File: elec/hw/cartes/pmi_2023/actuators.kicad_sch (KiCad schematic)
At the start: 43 parts, among them J1 con_servo, J2 con_servo, J3 con_servo, J4 con_servo, U23 PCA9685PW, U24 SN74LVC1T45DBV, U25 SN74LVC1T45DBV, U26 SN74LVC1T45DBV, U27 SN74LVC1T45DBV

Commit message: front and back tof added, selector changed, ready to route
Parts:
- R54, R55, R56, R57, R58, R59, R60, R61: JLCPCB C21189 -> C431718
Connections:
- net led_vbatt_error: now also BATT_LOW1.1 (K); no longer BATT_LOW1.C
- net at R64.2: now also BATT_LOW1.2 (A); no longer BATT_LOW1.A

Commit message: wip
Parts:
- R62, R63, R64: Specification 1k 0603 1% 100mW -> 10k 0603 1% 100mW; mouser (none) -> 603-RC0603FR-10100KL

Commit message: wip
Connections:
- net led_RGB_b_3v3: now also U23.20 (LED13); no longer U23.21 (LED14)
- net led_RGB_g_3v3: now also U23.21 (LED14); no longer U23.20 (LED13)
- net at R75.2: now also D1.2 (C_GREEN); no longer D1.1 (C_BLUE)
- net at R76.2: now also D1.1 (C_BLUE); no longer D1.2 (C_GREEN)
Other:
- moved on the sheet: R75, R76
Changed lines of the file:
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@@
+	(wire
+		(pts
+			(xy 220.98 50.8) (xy 232.41 50.8)
+		)
+		(stroke
+			(width 0)
+			(type default)
+		)
+	)
 	(wire
 		(pts
@@
 	(wire
 		(pts
-			(xy 229.87 45.72) (xy 232.41 45.72)
-		)
-		(stroke
-			(width 0)
-			(type default)
-		)
-	)
-	(wire
-		(pts
 			(xy 58.42 29.21) (xy 58.42 72.39)
 		)
@@
 	(wire
 		(pts
-			(xy 195.58 50.8) (xy 213.36 50.8)
+			(xy 194.31 45.72) (xy 222.25 45.72)
 		)
 		(stroke
@@
 	(wire
 		(pts
+			(xy 229.87 45.72) (xy 232.41 45.72)
+		)
+		(stroke
+			(width 0)
+			(type default)
+		)
+	)
+	(wire
+		(pts
 			(xy 137.16 21.59) (xy 137.16 29.21)
 		)
@@
 	(wire
 		(pts
-			(xy 220.98 50.8) (xy 232.41 50.8)
-		)
-		(stroke
-			(width 0)
-			(type default)
-		)
-	)
-	(wire
-		(pts
 			(xy 97.79 72.39) (xy 114.3 72.39)
 		)
@@
 	(wire
 		(pts
-			(xy 195.58 45.72) (xy 222.25 45.72)
+			(xy 194.31 50.8) (xy 213.36 50.8)
 		)
 		(stroke
@@
 		)
 	)
-	(label "led_RGB_g_3v3"
+	(label "led_RGB_b_3v3"
 		(at 99.06 69.85 0)
 		(fields_autoplaced yes)
@@
 	)
 	(label "led_RGB_b_3v3"
-		(at 195.58 50.8 0)
+		(at 194.31 45.72 0)
 		(fields_autoplaced yes)
 		(effects
@@
 	)
 	(label "led_RGB_g_3v3"
-		(at 195.58 45.72 0)
+		(at 194.31 50.8 0)
 		(fields_autoplaced yes)
 		(effects
@@
 		)
 	)
-	(label "led_RGB_b_3v3"
+	(label "led_RGB_g_3v3"
 		(at 99.06 72.39 0)
 		(fields_autoplaced yes)
@@
 	(symbol
 		(lib_id "cocotter_resistors:R_51R_0603_1%")
+		(at 226.06 45.72 90)
+		(unit 1)
+		(exclude_from_sim no)
+		(in_bom yes)
+		(on_board yes)
+		(dnp no)
+		(property "Reference" "R75"
+			(at 226.06 43.18 90)
+			(effects
+				(font
+					(size 1.27 1.27)
+				)
+			)
+		)
+		(property "Value" "51R 1%"
+			(at 226.06 48.26 90)
+			(effects
+				(font
+					(size 1.27 1.27)
+				)
+			)
+		)
+		(property "Footprint" "cocotter_resistor:r0603_reflow"
+			(at 226.06 47.498 90)
+			(effects
+				(font
+					(size 1.27 1.27)
+				)
+				(hide yes)
+			)
+		)
+		(property "Datasheet" "~"
+			(at 226.06 45.72 0)
+			(effects
+				(font
+					(size 1.27 1.27)
+				)
+				(hide yes)
+			)
+		)
+		(property "Description" ""
+			(at 226.06 45.72 0)
+			(effects
+				(font
+					(size 1.27 1.27)
+				)
+				(hide yes)
+			)
+		)
+		(property "Specification" "51R 0603 1% 100mW"
+			(at 226.06 45.72 0)
+			(effects
+				(font
+					(size 1.27 1.27)
+				)
+				(hide yes)
+			)
+		)
+		(property "mouser" ""
+			(at 226.06 45.72 0)
+			(effects
+				(font
+					(size 1.27 1.27)
+				)
+				(hide yes)
+			)
+		)
+		(property "JLCPCB" ""
+			(at 226.06 45.72 0)
+			(effects
+				(font
+					(size 1.27 1.27)
+				)
+				(hide yes)
+			)
+		)
+		(pin "2"
+		)
+		(pin "1"
+		)
+		(instances
+			(project "pmi_2023"
+				(path "/334a657f-c66c-4260-9567-14f1c99913d7/76b412a5-2e5b-49f9-bfc4-2fef81997c2b"
+					(reference "R75")
+					(unit 1)
+				)
+			)
+		)
+	)
+	(symbol
+		(lib_id "cocotter_resistors:R_51R_0603_1%")
 		(at 217.17 50.8 90)
 		(unit 1)
@@
 		(on_board yes)
 		(dnp no)
-		(property "Reference" "R75"
+		(property "Reference" "R76"
 			(at 217.17 48.26 90)
 			(effects
@@
 			(effects
 				(font
-					(size 1.27 1.27)
-				)
-				(hide yes)
-			)
-		)
-		(pin "2"
-		)
-		(pin "1"
-		)
-		(instances
-			(project "pmi_2023"
-				(path "/334a657f-c66c-4260-9567-14f1c99913d7/76b412a5-2e5b-49f9-bfc4-2fef81997c2b"
-					(reference "R75")
-					(unit 1)
-				)
-			)
-		)
-	)
-	(symbol
-		(lib_id "cocotter_resistors:R_51R_0603_1%")
-		(at 226.06 45.72 90)
-		(unit 1)
-		(exclude_from_sim no)
-		(in_bom yes)
-		(on_board yes)
-		(dnp no)
-		(property "Reference" "R76"
-			(at 226.06 43.18 90)
-			(effects
-				(font
-					(size 1.27 1.27)
-				)
-			)
-		)
-		(property "Value" "51R 1%"
-			(at 226.06 48.26 90)
-			(effects
-				(font
-					(size 1.27 1.27)
-				)
-			)
-		)
-		(property "Footprint" "cocotter_resistor:r0603_reflow"
-			(at 226.06 47.498 90)
-			(effects
-				(font
-					(size 1.27 1.27)
-				)
-				(hide yes)
-			)
-		)
-		(property "Datasheet" "~"
-			(at 226.06 45.72 0)
-			(effects
-				(font
-					(size 1.27 1.27)
-				)
-				(hide yes)
-			)
-		)
-		(property "Description" ""
-			(at 226.06 45.72 0)
-			(effects
-				(font
-					(size 1.27 1.27)
-				)
-				(hide yes)
-			)
-		)
-		(property "Specification" "51R 0603 1% 100mW"
-			(at 226.06 45.72 0)
-			(effects
-				(font
-					(size 1.27 1.27)
-				)
-				(hide yes)
-			)
-		)
-		(property "mouser" ""
-			(at 226.06 45.72 0)
-			(effects
-				(font
-					(size 1.27 1.27)
-				)
-				(hide yes)
-			)
-		)
-		(property "JLCPCB" ""
-			(at 226.06 45.72 0)
-			(effects
-				(font

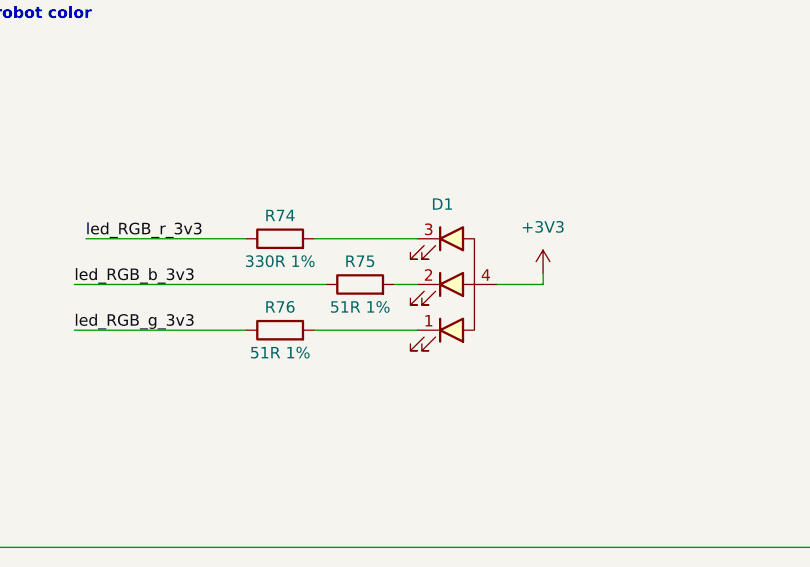
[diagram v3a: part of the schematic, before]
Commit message: added oled display power supply res selectors, jlcpcb refs : wip
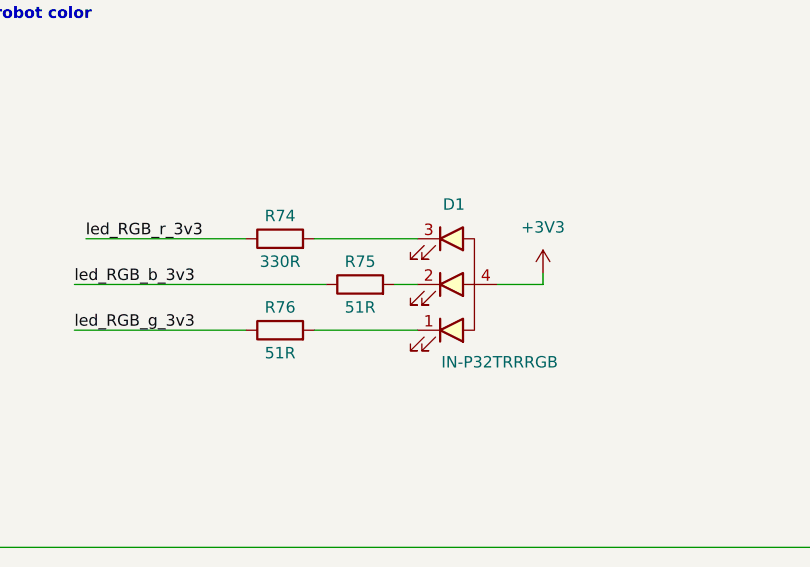
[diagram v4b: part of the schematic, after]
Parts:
- BATT_OK1: value red, 0603 -> white, 0603
- C14, C23, C24, C25, C26: symbol cocotter_capacitors:C_10µF_16V_0805_X5R -> cocotter_capacitors:C_10µF_25V_0805_X5R; Specification 10µF 25V X5R 0805 -> 10µF 25V X7R 0805
- D1: value ~ -> IN-P32TRRRGB; JLCPCB (none) -> C7288909
- R74: value 330R 1% -> 330R; JLCPCB (none) -> C23138
- R75, R76: value 51R 1% -> 51R; JLCPCB (none) -> C23197
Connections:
- net led_vbatt_ok: now also BATT_OK1.1 (K); no longer BATT_OK1.C
- net at R62.2: now also BATT_OK1.2 (A); no longer BATT_OK1.A
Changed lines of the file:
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@@
 			)
 		)
-		(property "Description" "Unpolarized capacitor"
+		(property "Description" "Unpolarized capacitor tol +/-10%"
 			(at 60.96 166.37 0)
 			(effects
@@
 			)
 		)
-		(property "Description" "Unpolarized capacitor"
+		(property "Description" "Unpolarized capacitor tol +/-10%"
 			(at 60.96 129.54 0)
 			(effects
@@
 	)
 	(symbol
-		(lib_id "cocotter_capacitors:C_10µF_16V_0805_X5R")
+		(lib_id "cocotter_capacitors:C_10µF_25V_0805_X5R")
 		(at 76.2 149.86 0)
 		(unit 1)
@@
 			)
 		)
-		(property "Description" ""
+		(property "Description" "Unpolarized capacitor"
 			(at 76.2 149.86 0)
 			(effects
@@
 			)
 		)
-		(property "Specification" "10µF 25V X5R 0805 "
+		(property "Specification" "10µF 25V X7R 0805 "
 			(at 76.2 149.86 0)
 			(effects
@@
 	)
 	(symbol
-		(lib_id "cocotter_capacitors:C_10µF_16V_0805_X5R")
+		(lib_id "cocotter_capacitors:C_10µF_25V_0805_X5R")
 		(at 223.52 157.48 0)
 		(unit 1)
@@
 			)
 		)
-		(property "Description" ""
+		(property "Description" "Unpolarized capacitor"
 			(at 223.52 157.48 0)
 			(effects
@@
 			)
 		)
-		(property "Specification" "10µF 25V X5R 0805 "
+		(property "Specification" "10µF 25V X7R 0805 "
 			(at 223.52 157.48 0)
 			(effects
@@
 			)
 		)
-		(property "Value" "51R 1%"
+		(property "Value" "51R"
 			(at 226.06 48.26 90)
 			(effects
@@
 			)
 		)
-		(property "Description" ""
+		(property "Description" "Resistor"
 			(at 226.06 45.72 0)
 			(effects
@@
 			)
 		)
-		(property "JLCPCB" ""
+		(property "JLCPCB" "C23197"
 			(at 226.06 45.72 0)
 			(effects
@@
 			)
 		)
-		(property "Value" "51R 1%"
+		(property "Value" "51R"
 			(at 217.17 53.34 90)
 			(effects
@@
 			)
 		)
-		(property "Description" ""
+		(property "Description" "Resistor"
 			(at 217.17 50.8 0)
 			(effects
@@
 			)
 		)
-		(property "JLCPCB" ""
+		(property "JLCPCB" "C23197"
 			(at 217.17 50.8 0)
 			(effects
@@
 			)
 		)
-		(property "Description" "Unpolarized capacitor"
+		(property "Description" "Unpolarized capacitor tol +/-10%"
 			(at 21.59 129.54 0)
 			(effects
@@
 			)
 		)
-		(property "Description" "Unpolarized capacitor"
+		(property "Description" "Unpolarized capacitor tol +/-10%"
 			(at 21.59 166.37 0)
 			(effects
@@
 			)
 		)
-		(property "Description" "Unpolarized capacitor"
+		(property "Description" "Unpolarized capacitor tol +/-10%"
 			(at 168.91 137.16 0)
 			(effects
@@
 			)
 		)
-		(property "Description" "Unpolarized capacitor"
+		(property "Description" "Unpolarized capacitor tol +/-10%"
 			(at 168.91 99.06 0)
 			(effects
@@
 			)
 		)
-		(property "Description" "Unpolarized capacitor"
+		(property "Description" "Unpolarized capacitor tol +/-10%"
 			(at 87.63 25.4 0)
 			(effects
@@
 	)
 	(symbol
-		(lib_id "cocotter_capacitors:C_10µF_16V_0805_X5R")
+		(lib_id "cocotter_capacitors:C_10µF_25V_0805_X5R")
 		(at 223.52 119.38 0)
 		(unit 1)
@@
 			)
 		)
-		(property "Description" ""
+		(property "Description" "Unpolarized capacitor"
 			(at 223.52 119.38 0)
 			(effects
@@
 			)
 		)
-		(property "Specification" "10µF 25V X5R 0805 "
+		(property "Specification" "10µF 25V X7R 0805 "
 			(at 223.52 119.38 0)
 			(effects
@@
 			)
 		)
-		(property "Description" "Unpolarized capacitor"
+		(property "Description" "Unpolarized capacitor tol +/-10%"
 			(at 208.28 99.06 0)
 			(effects
@@
 	)
 	(symbol
-		(lib_id "cocotter_capacitors:C_10µF_16V_0805_X5R")
+		(lib_id "cocotter_capacitors:C_10µF_25V_0805_X5R")
 		(at 76.2 186.69 0)
 		(unit 1)
@@
 			)
 		)
-		(property "Description" ""
+		(property "Description" "Unpolarized capacitor"
 			(at 76.2 186.69 0)
 			(effects
@@
 			)
 		)
-		(property "Specification" "10µF 25V X5R 0805 "
+		(property "Specification" "10µF 25V X7R 0805 "
 			(at 76.2 186.69 0)
 			(effects
@@
 	)
 	(symbol
-		(lib_id "cocotter_capacitors:C_10µF_16V_0805_X5R")
+		(lib_id "cocotter_capacitors:C_10µF_25V_0805_X5R")
 		(at 105.41 25.4 0)
 		(unit 1)
@@
 			)
 		)
-		(property "Description" ""
+		(property "Description" "Unpolarized capacitor"
 			(at 105.41 25.4 0)
 			(effects
@@
 			)
 		)
-		(property "Specification" "10µF 25V X5R 0805 "
+		(property "Specification" "10µF 25V X7R 0805 "
 			(at 105.41 25.4 0)
 			(effects
@@
 			)
 		)
-		(property "Value" "330R 1%"
+		(property "Value" "330R"
 			(at 217.17 43.18 90)
 			(effects
@@
 			)
 		)
-		(property "Description" ""
+		(property "Description" "Resistor"
 			(at 217.17 40.64 0)
 			(effects
@@
 			)
 		)
-		(property "JLCPCB" ""
+		(property "JLCPCB" "C23138"
 			(at 217.17 40.64 0)
 			(effects
@@
 	(symbol
 		(lib_id "cocotter_diodes:IN-P32TRRRGB")
-		(at 236.22 45.72 0)
+		(at 237.49 45.72 0)
 		(unit 1)
 		(exclude_from_sim no)
@@
 		(on_board yes)
 		(dnp no)
-		(fields_autoplaced yes)
 		(property "Reference" "D1"
-			(at 235.204 36.83 0)
+			(at 236.474 36.83 0)
 			(effects
 				(font
@@
 			)
 		)
-		(property "Value" "~"
-			(at 236.22 40.64 0)
+		(property "Value" "IN-P32TRRRGB"
+			(at 241.554 54.356 0)
 			(effects
 				(font
@@
 		)
 		(property "Footprint" "cocotter_diodes:3528_PLCC-Reverse_mount"
-			(at 236.22 40.64 0)
+			(at 237.49 40.64 0)
 			(effects
 				(font
@@
 		)
 		(property "Datasheet" ""
-			(at 236.22 40.64 0)
+			(at 237.49 40.64 0)
 			(effects
 				(font
@@
 			)
 		)
-		(property "Description" ""
-			(at 236.22 45.72 0)
+		(property "Description" "RGB LED, reverse mount"
+			(at 237.49 45.72 0)
+			(effects
+				(font
+					(size 1.27 1.27)
+				)
+				(hide yes)
+			)
+		)
+		(property "JLCPCB" "C7288909"
+			(at 237.49 45.72 0)
 			(effects
 				(font
@@
 			)
 		)
-		(property "Value" "red, 0603"
+		(property "Value" "white, 0603"
 			(at 168.91 40.64 0)
 			(effects
@@
 			)
 		)
-		(property "Description" ""
+		(property "Description" "Light emitting diode, white, Vf=[2.6V; 3.1V]"
 			(at 166.37 40.64 0)
 			(effects
@@
 			)
 		)
-		(pin "C"
+		(pin "1"
 		)
-		(pin "A"
+		(pin "2"
 		)
 		(instances
@@
 			)
 		)
-		(property "Description" "Unpolarized capacitor"
+		(property "Description" "Unpolarized capacitor tol +/-10%"
 			(at 208.28 137.16 0)
 			(effects

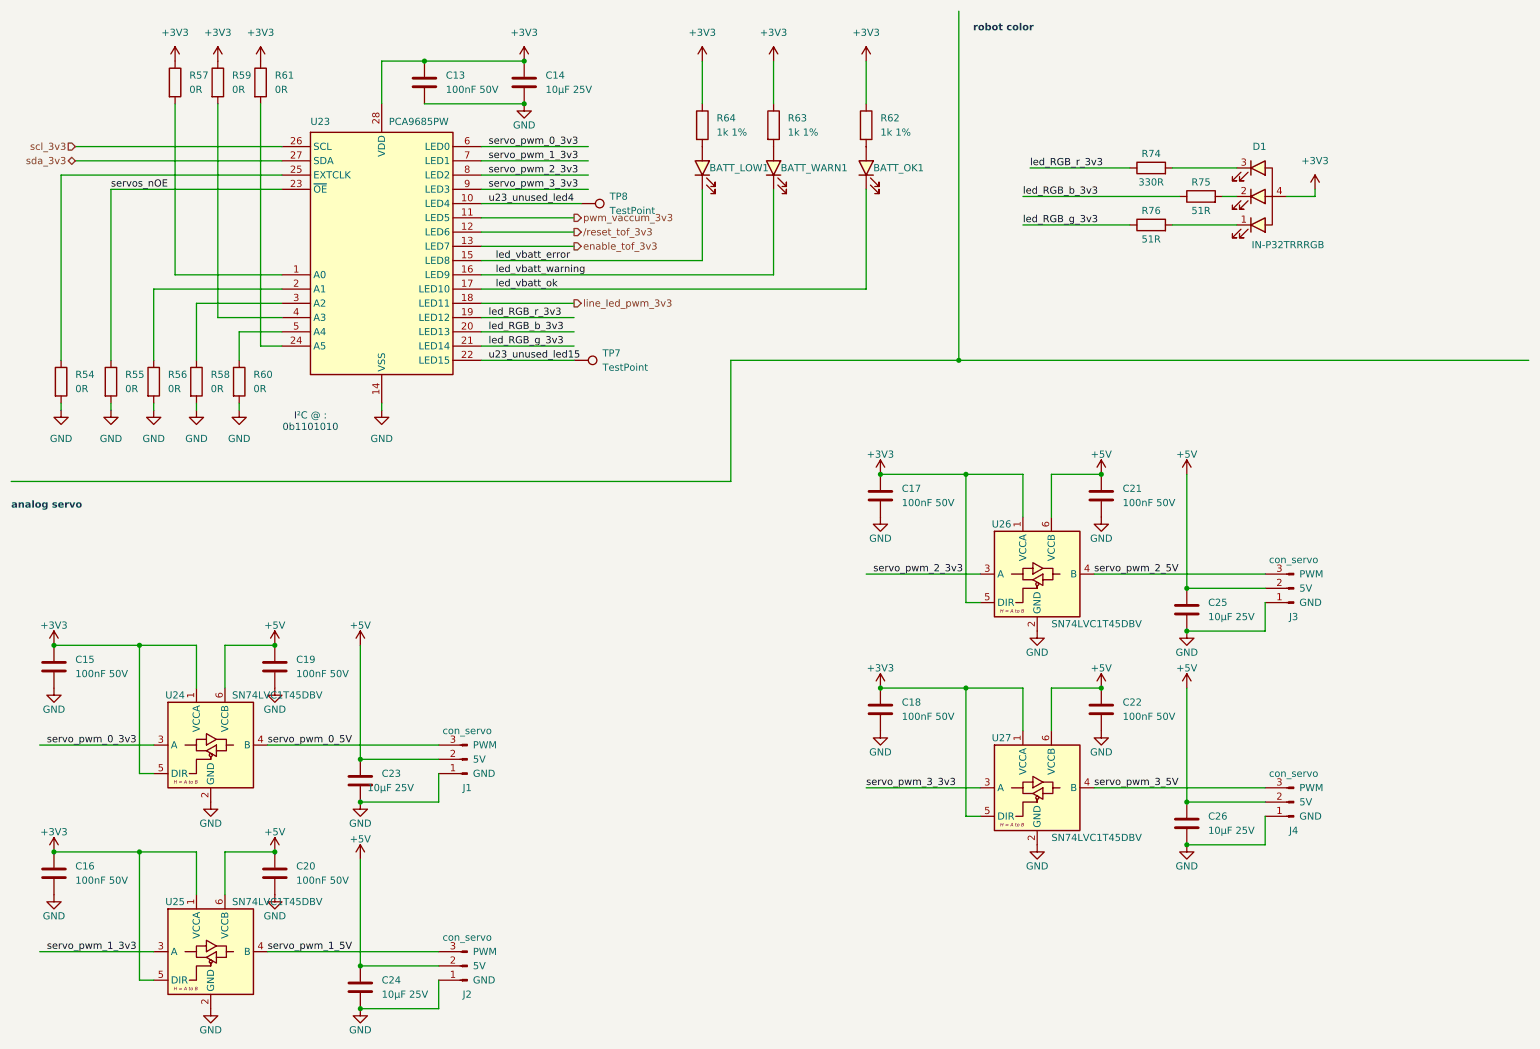
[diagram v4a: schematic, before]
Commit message: reset button added to esp32 reset. uart prog connector replaces ftdi one
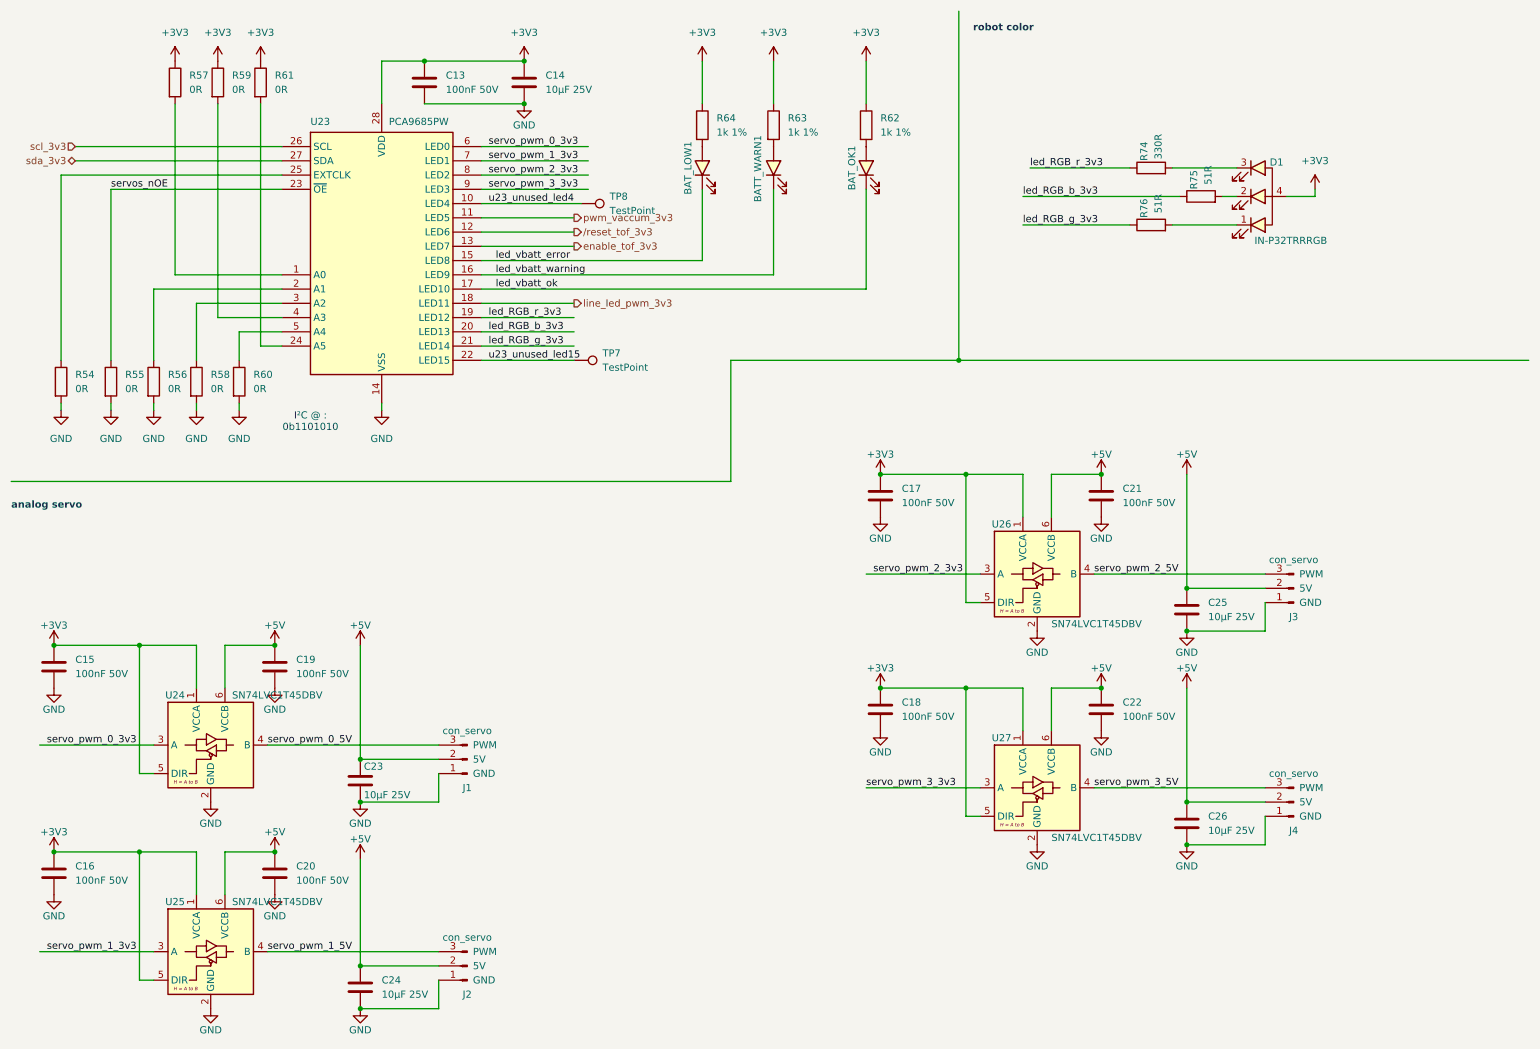
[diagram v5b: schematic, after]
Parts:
- BAT_LOW1: renamed from BATT_LOW1; footprint cocotter_diodes:LED_0603_1608Metric -> (none)
- BAT_OK1: renamed from BATT_OK1; footprint cocotter_diodes:LED_0603_1608Metric -> (none)
- D1: footprint cocotter_diodes:3528_PLCC-Reverse_mount -> (none)

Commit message: pmi2023 : drc cleanup
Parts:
- BAT_LOW1, BAT_OK1: footprint (none) -> cocotter_diodes:LED_0603_1608Metric
- BAT_WARN1: renamed from BATT_WARN1; DIGIKEY_REF (none) -> 150060YS55040
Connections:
- net led_vbatt_error: now also BAT_LOW1.C; no longer BAT_LOW1.1 (C)
- net led_vbatt_ok: now also BAT_OK1.C; no longer BAT_OK1.1 (C)
- net at R62.2: now also BAT_OK1.A; no longer BAT_OK1.2 (A)
- net at R64.2: now also BAT_LOW1.A; no longer BAT_LOW1.2 (A)
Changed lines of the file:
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@@
 			)
 		)
-		(property "Footprint" ""
+		(property "Footprint" "cocotter_diodes:LED_0603_1608Metric"
 			(at 137.16 40.64 0)
 			(effects
@@
 			)
 		)
-		(pin "2"
+		(pin "C"
 		)
-		(pin "1"
+		(pin "A"
 		)
 		(instances
@@
 		(on_board yes)
 		(dnp no)
-		(property "Reference" "BATT_WARN1"
+		(property "Reference" "BAT_WARN1"
 			(at 147.066 34.798 0)
+			(do_not_autoplace yes)
 			(effects
 				(font
@@
 			)
 		)
-		(property "Description" ""
+		(property "Description" "Light emitting diode, Yellow, Vf=[2V; 2.4V]"
 			(at 149.86 40.64 0)
 			(effects
@@
 			)
 		)
-		(property "DIGIKEY_REF" ""
+		(property "DIGIKEY_REF" "150060YS55040"
 			(at 151.13 40.64 0)
 			(effects
@@
 			(project "pmi_2023"
 				(path "/334a657f-c66c-4260-9567-14f1c99913d7/76b412a5-2e5b-49f9-bfc4-2fef81997c2b"
-					(reference "BATT_WARN1")
+					(reference "BAT_WARN1")
 					(unit 1)
 				)
@@
 		(property "Reference" "BAT_OK1"
 			(at 163.83 40.64 0)
+			(do_not_autoplace yes)
 			(effects
 				(font
@@
 			)
 		)
-		(property "Footprint" ""
+		(property "Footprint" "cocotter_diodes:LED_0603_1608Metric"
 			(at 166.37 40.64 0)
 			(effects
@@
 			)
 		)
-		(pin "1"
+		(pin "A"
 		)
-		(pin "2"
+		(pin "C"
 		)
 		(instances

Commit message: small changes
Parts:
- D1: footprint (none) -> cocotter_diodes:3528_PLCC-Reverse_mount
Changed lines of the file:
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@@
 			)
 		)
-		(property "Footprint" ""
+		(property "Footprint" "cocotter_diodes:3528_PLCC-Reverse_mount"
 			(at 237.49 45.72 0)
 			(effects
